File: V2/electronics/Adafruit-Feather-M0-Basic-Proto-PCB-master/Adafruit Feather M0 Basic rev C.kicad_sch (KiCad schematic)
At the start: 33 parts, among them SW1 SPST_TACT-KMR2, U2 SPX3819-3.3, U3 MCP73831T-2ACI/OT, X1 JSTPH, X2 32.768, X3 microUSB

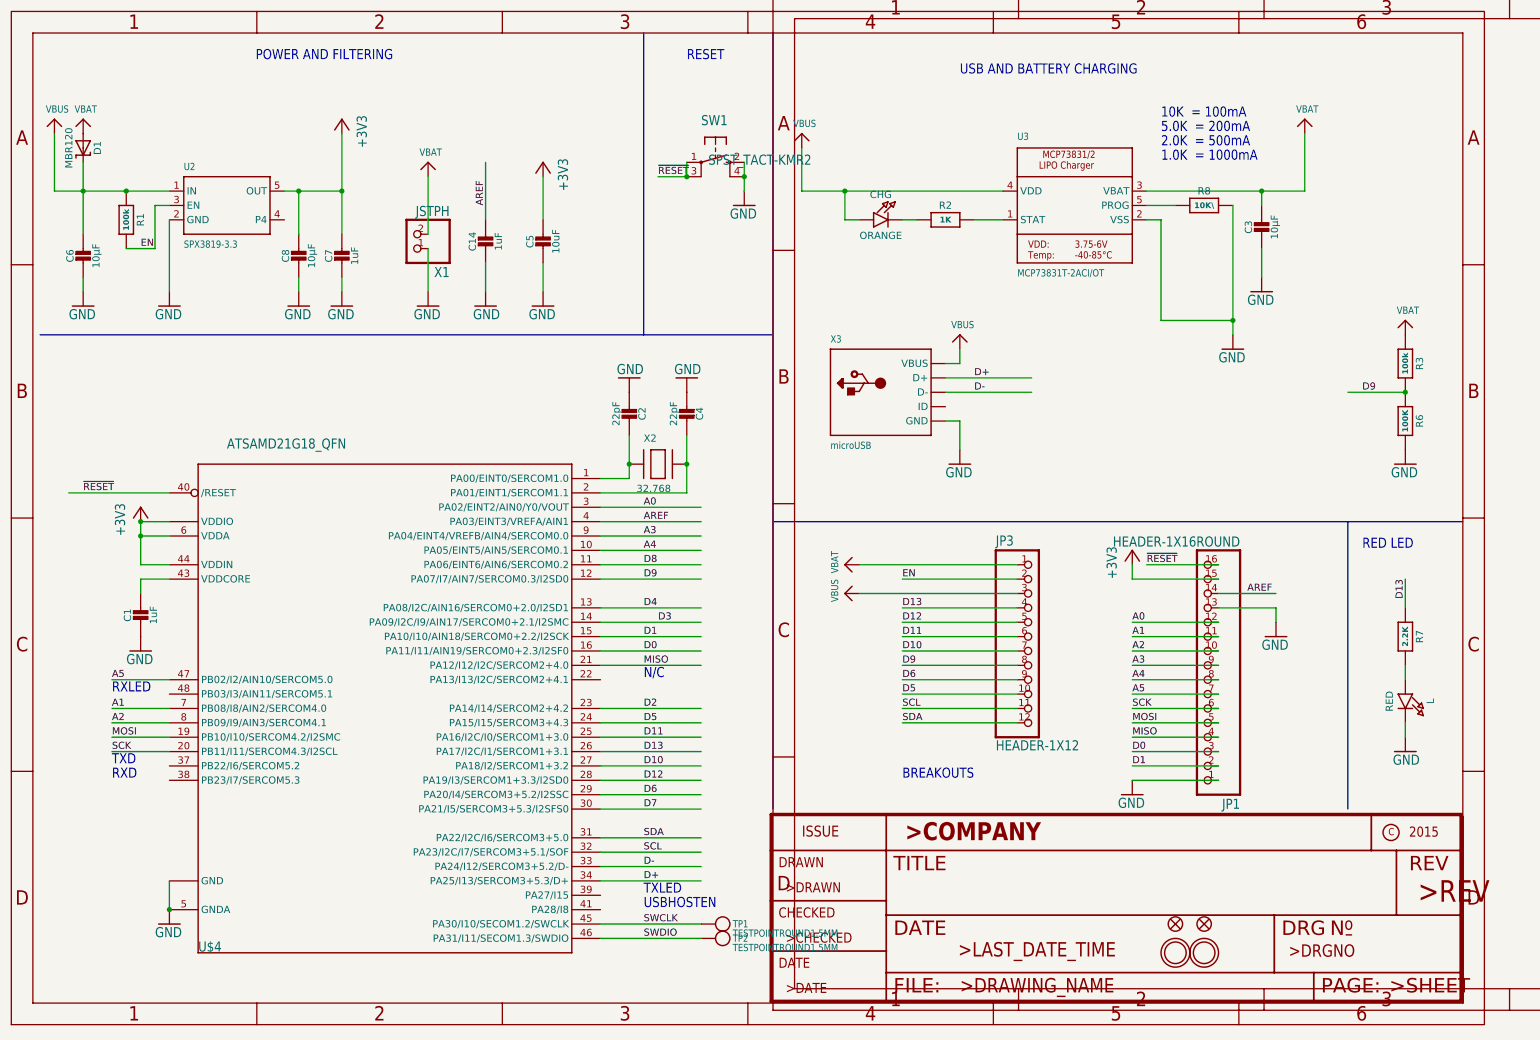
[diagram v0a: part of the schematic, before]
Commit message: main sch assigning footprints 06 04 22
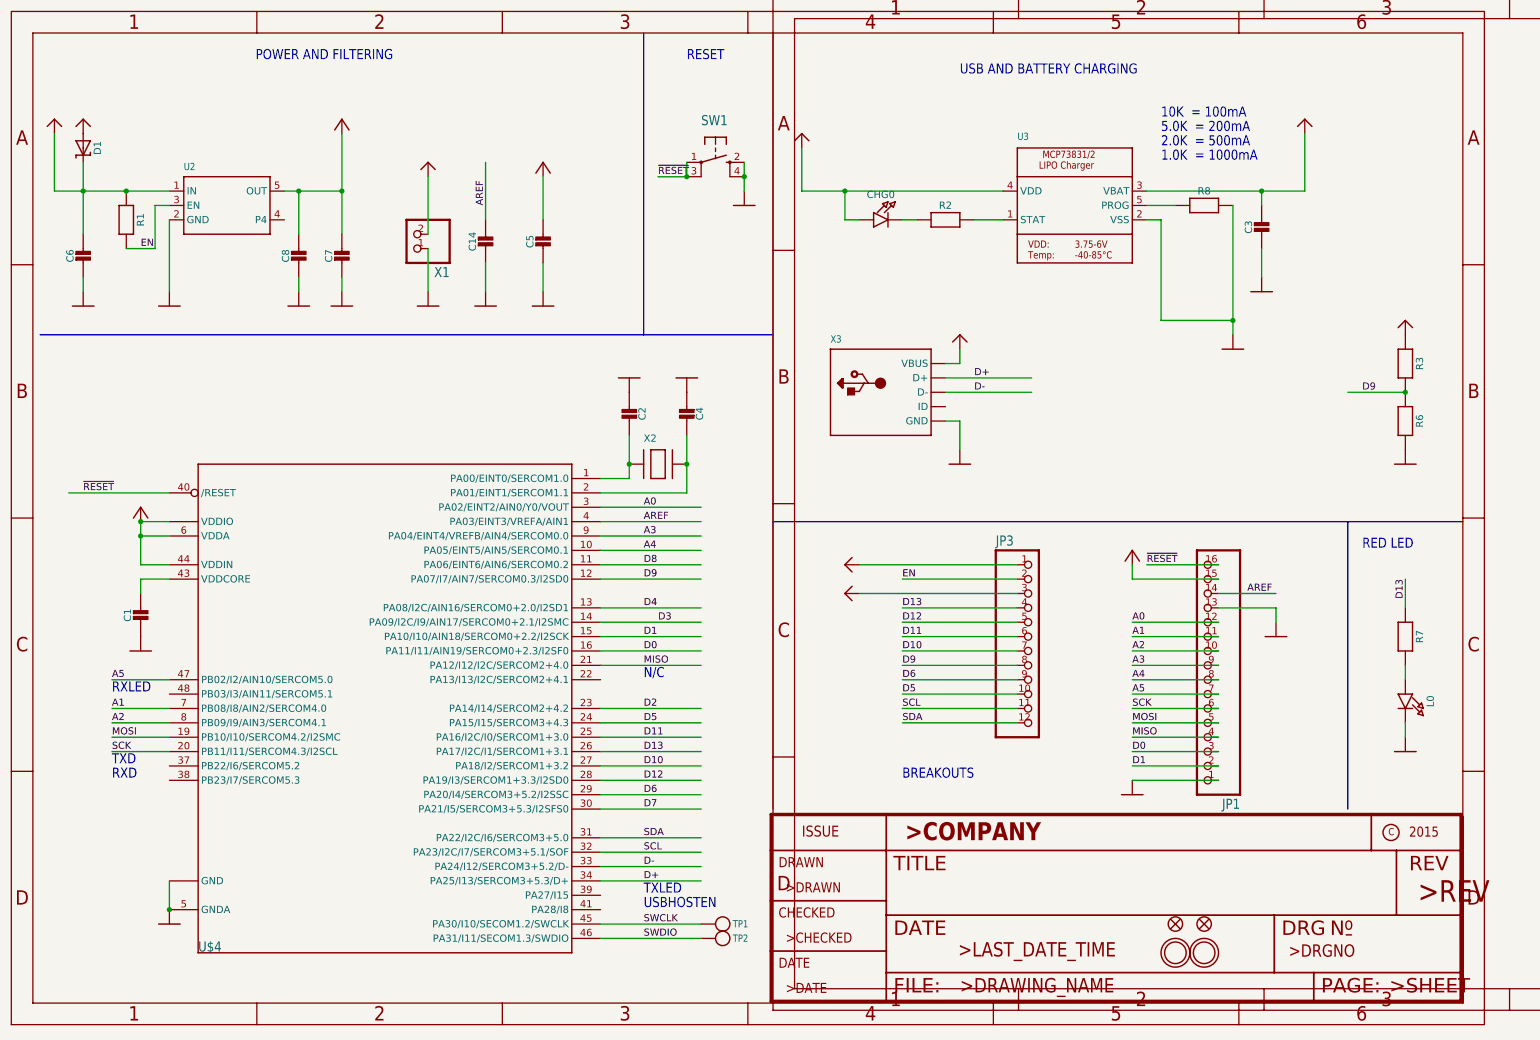
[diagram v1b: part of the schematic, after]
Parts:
- removed CHG: ORANGE, CHIPLED_0805_NOOUTLINE, symbol Adafruit Feather M0 Basic rev C-eagle-import:LED0805_NOOUTLINE
- removed L: RED, CHIPLED_0805_NOOUTLINE, symbol Adafruit Feather M0 Basic rev C-eagle-import:LED0805_NOOUTLINE
- added CHG0, L0: (no value), symbol Adafruit Feather M0 Basic rev C-eagle-import:LED0805_NOOUTLINE
- C1, C14, C7: value 1uF -> (none); footprint 0603-NO -> (none)
- C2, C4: value 22pF -> (none); footprint 0603-NO -> (none)
- C3, C6, C8: value 10µF -> (none); footprint 0805-NO -> (none)
- C5: value 10uF -> (none); footprint 0805-NO -> (none)
- D1: value MBR120 -> (none); footprint SOD-123 -> (none)
- JP1: value HEADER-1X16ROUND -> (none); footprint 1X16_ROUND -> (none)
- JP3: value HEADER-1X12 -> (none); footprint 1X12_ROUND -> (none)
- R1, R3: value 100k -> (none); footprint 0603-NO -> (none)
- R2: value 1K -> (none); footprint 0603-NO -> (none)
- R6: value 100K -> (none); footprint 0603-NO -> (none)
- R7: value 2.2K -> (none); footprint 0603-NO -> (none)
- R8: value 10K\ -> (none); footprint 0603-NO -> (none)
- SW1: value SPST_TACT-KMR2 -> (none); footprint KMR2 -> (none)
- TP1, TP2: value TESTPOINTROUND1.5MM -> (none); footprint TESTPOINT_ROUND_1.5MM -> (none)
- U$31, U$32: value MOUNTINGHOLE2.5 -> (none); footprint MOUNTINGHOLE_2.5_PLATED -> (none)
- U$34, U$35: value FIDUCIAL{dblquote}{dblquote} -> (none); footprint FIDUCIAL_1MM -> (none)
- U$4: value ATSAMD21G18_QFN -> (none); footprint TQFN48_7MM -> (none)
- U2: value SPX3819-3.3 -> (none); footprint SOT23-5 -> (none)
- U3: value MCP73831T-2ACI/OT -> (none); footprint SOT23-5 -> (none)
- X1: value JSTPH -> (none); footprint JSTPH2 -> (none)
- X2: value 32.768 -> (none); footprint XTAL3215 -> (none)
- X3: value microUSB -> (none); footprint 4UCONN_20329_V2 -> (none)
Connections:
- net GND: now also L0.C
- net VBUS: now also CHG0.A
- net at R7.2: now also L0.A
- net at R2.1: now also CHG0.C

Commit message: main sch footprints 07 04 22
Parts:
- C1, C14, C7: value (none) -> 1uF; footprint (none) -> Adafruit Feather M0 Basic rev C:0603-NO
- C2, C4: value (none) -> 22pF; footprint (none) -> Adafruit Feather M0 Basic rev C:0603-NO
- C3, C6, C8: value (none) -> 10µF; footprint (none) -> Adafruit Feather M0 Basic rev C:0805-NO
- C5: value (none) -> 10uF; footprint (none) -> Adafruit Feather M0 Basic rev C:0805-NO
- CHG0: value (none) -> ORANGE; footprint (none) -> Adafruit Feather M0 Basic rev C:CHIPLED_0805_NOOUTLINE
- D1: value (none) -> MBR120; footprint (none) -> Adafruit Feather M0 Basic rev C:SOD-123
- JP1: value (none) -> HEADER-1X16ROUND; footprint (none) -> Adafruit Feather M0 Basic rev C:1X16_ROUND
- JP3: value (none) -> HEADER-1X12; footprint (none) -> Adafruit Feather M0 Basic rev C:1X12_ROUND
- L0: value (none) -> RED; footprint (none) -> Adafruit Feather M0 Basic rev C:CHIPLED_0805_NOOUTLINE
- R1, R3: value (none) -> 100k; footprint (none) -> Adafruit Feather M0 Basic rev C:0603-NO
- R2: value (none) -> 1K; footprint (none) -> Adafruit Feather M0 Basic rev C:0603-NO
- R6: value (none) -> 100K; footprint (none) -> Adafruit Feather M0 Basic rev C:0603-NO
- R7: value (none) -> 2.2K; footprint (none) -> Adafruit Feather M0 Basic rev C:0603-NO
- R8: value (none) -> 10K\; footprint (none) -> Adafruit Feather M0 Basic rev C:0603-NO
- SW1: value (none) -> SPST_TACT-KMR2; footprint (none) -> Adafruit Feather M0 Basic rev C:KMR2
- TP1, TP2: value (none) -> TESTPOINTROUND1.5MM; footprint (none) -> Adafruit Feather M0 Basic rev C:TESTPOINT_ROUND_1.5MM
- U$31, U$32: value (none) -> MOUNTINGHOLE2.5; footprint (none) -> Adafruit Feather M0 Basic rev C:MOUNTINGHOLE_2.5_PLATED
- U$34, U$35: value (none) -> FIDUCIAL{dblquote}{dblquote}; footprint (none) -> Adafruit Feather M0 Basic rev C:FIDUCIAL_1MM
- U$4: value (none) -> ATSAMD21G18_QFN; footprint (none) -> Adafruit Feather M0 Basic rev C:TQFN48_7MM
- U2: value (none) -> SPX3819-3.3; footprint (none) -> Adafruit Feather M0 Basic rev C:SOT23-5
- U3: value (none) -> MCP73831T-2ACI/OT; footprint (none) -> Adafruit Feather M0 Basic rev C:SOT23-5
- X1: value (none) -> JSTPH; footprint (none) -> Adafruit Feather M0 Basic rev C:JSTPH2
- X2: value (none) -> 32.768; footprint (none) -> Adafruit Feather M0 Basic rev C:XTAL3215
- X3: value (none) -> microUSB; footprint (none) -> Adafruit Feather M0 Basic rev C:4UCONN_20329_V2
